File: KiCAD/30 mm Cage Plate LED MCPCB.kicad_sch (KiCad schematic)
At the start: 26 parts, among them IC1 AL8843QSP-13, J1 Conn_01x08_Socket, J2 0, M1 Fan, Q5 2x_p-channel, Q6 2x_p-channel

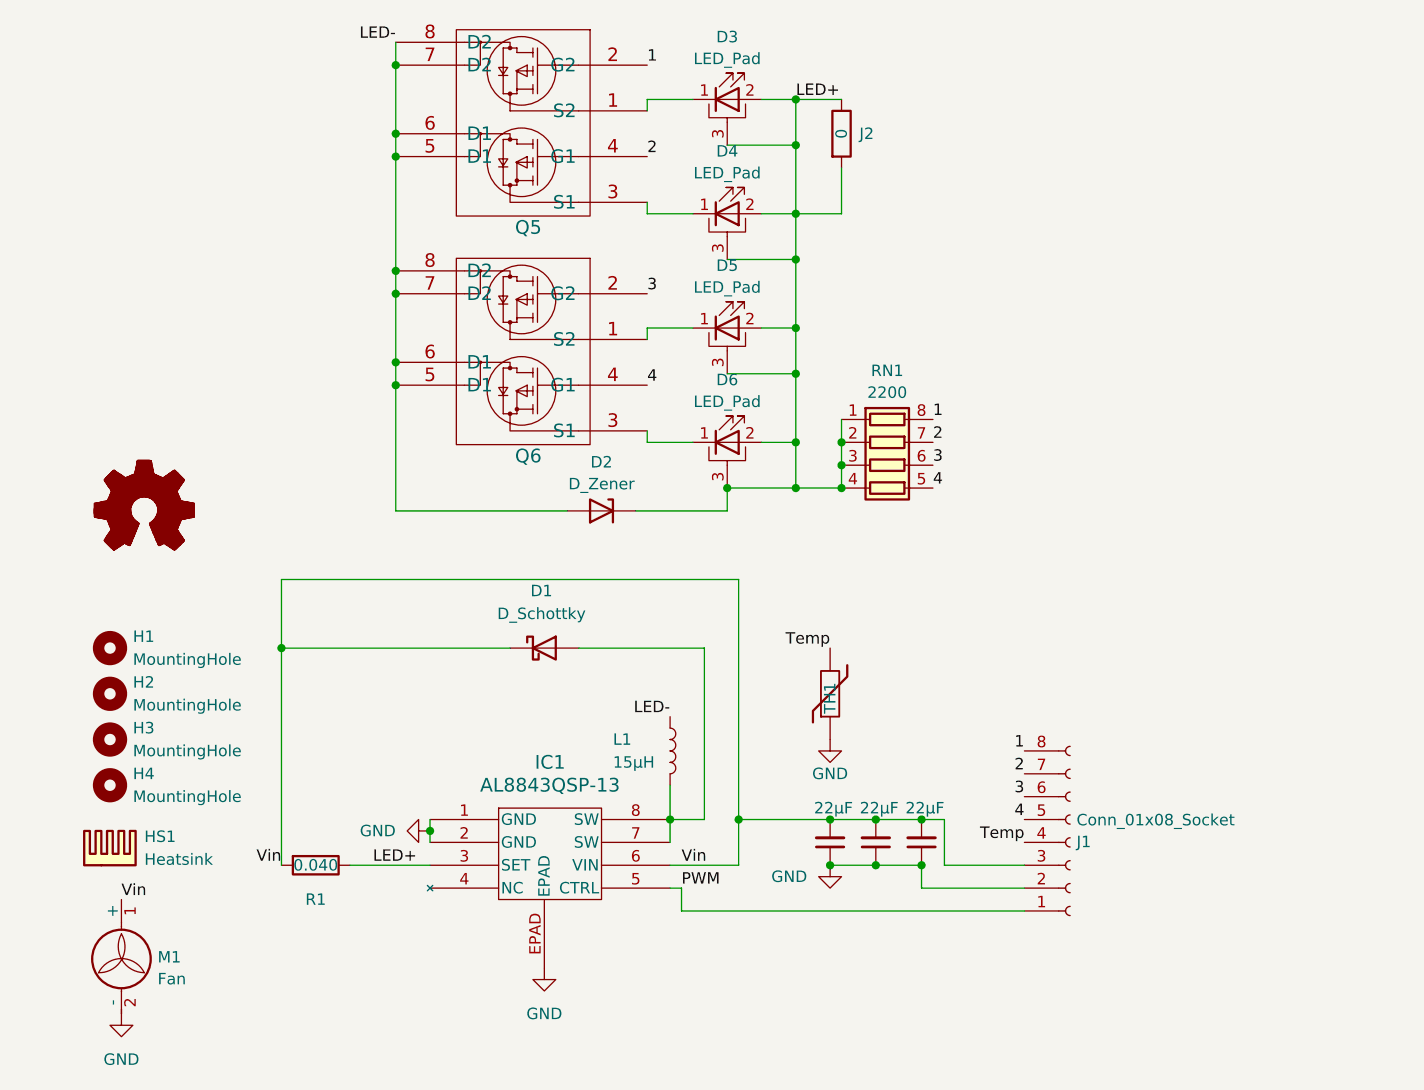
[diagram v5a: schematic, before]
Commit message: pmos mux connected - better conduction path
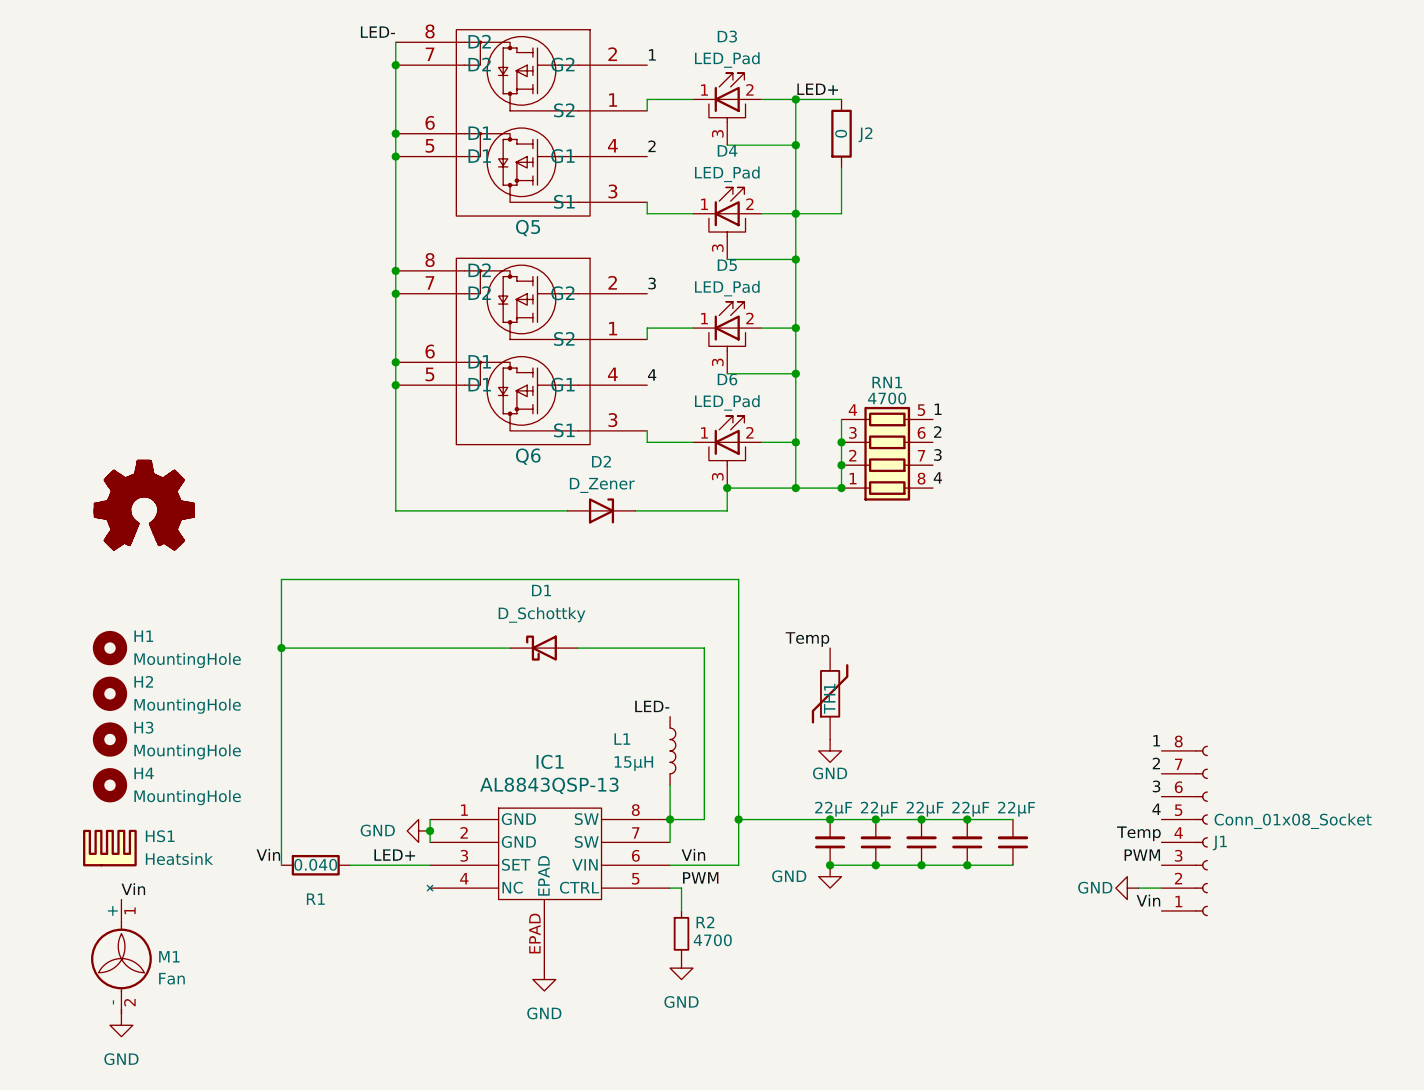
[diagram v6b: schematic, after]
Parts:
- added C4, C5: 22μF, Capacitor_SMD:C_0805_2012Metric, symbol Device:C_Small
- added R2: 4700, Resistor_SMD:R_0603_1608Metric, symbol Device:R_Small
- RN1: value 2200 -> 4700; footprint Resistor_SMD:R_Array_Convex_4x0603 -> Resistor_SMD:R_Array_Convex_4x1206; Part YC164-JR-072K2L -> YC324-JK-074K7L
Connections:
- net 1: now also RN1.5 (R4.2); no longer RN1.8 (R1.2)
- net 2: now also RN1.6 (R3.2); no longer RN1.7 (R2.2)
- net 3: now also RN1.7 (R2.2); no longer RN1.6 (R3.2)
- net 4: now also RN1.8 (R1.2); no longer RN1.5 (R4.2)
- net GND: now also C4.1, C5.1, R2.2
- net PWM: now also J1.3 (Pin_3), R2.1; no longer J1.1 (Pin_1)
- net Vin: now also J1.1 (Pin_1), C4.2, C5.2; no longer J1.3 (Pin_3)
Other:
- moved on the sheet: J1
